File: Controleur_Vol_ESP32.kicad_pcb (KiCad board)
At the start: 2 copper layers, 67 parts, among them J1 Conn_01x03, J10 Conn_01x03, J11 Conn_01x08, J12 Conn_01x03, J13 Conn_01x03, J14 Conn_01x04, J15 Screw_Terminal_01x02, J2 Conn_01x03, J3 Conn_01x03, J4 Conn_01x03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

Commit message: Correction erreurs liens
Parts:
- moved J13 77.0 mm to (243.8, 238.8)
- moved J11 63.0 mm to (116.8, 275.6)
- moved J15 56.9 mm to (215.9, 236.2)
- moved J12 53.6 mm to (233.7, 248.9)
- moved U4 52.4 mm to (139.5, 272.2)
- moved R15 44.1 mm to (218.4, 264.2)
- moved R12 40.8 mm to (127.0, 233.7)
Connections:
- U4 pad 10: ESC3_5V -> ESC4_5V
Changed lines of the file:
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@@
   )
   (setup
+    (stackup
+      (layer "F.SilkS" (type "Top Silk Screen"))
+      (layer "F.Paste" (type "Top Solder Paste"))
+      (layer "F.Mask" (type "Top Solder Mask") (thickness 0.01))
+      (layer "F.Cu" (type "copper") (thickness 0.035))
+      (layer "dielectric 1" (type "core") (thickness 1.51) (material "FR4") (epsilon_r 4.5) (loss_tangent 0.02))
+      (layer "B.Cu" (type "copper") (thickness 0.035))
+      (layer "B.Mask" (type "Bottom Solder Mask") (thickness 0.01))
+      (layer "B.Paste" (type "Bottom Solder Paste"))
+      (layer "B.SilkS" (type "Bottom Silk Screen"))
+      (copper_finish "Immersion gold")
+      (dielectric_constraints no)
+    )
     (pad_to_mask_clearance 0)
     (pcbplotparams
@@
   )
   (footprint "Library_JBO:LM298_CI" (layer "F.Cu")
-    (at 127.25 221.23)
+    (at 139.455 272.225)
     (property "Sheetfile" "Controleur_Vol_ESP32.kicad_sch")
     (property "Sheetname" "")
@@
       (net 39 "ESC3_5V") (pinfunction "OUT3") (pintype "output"))
     (pad "10" thru_hole oval (at 2 19.5) (size 2 3.2) (drill 0.8) (layers *.Cu *.Mask)
-      (net 39 "ESC3_5V") (pinfunction "OUT4") (pintype "output"))
+      (net 41 "ESC4_5V") (pinfunction "OUT4") (pintype "output"))
   )
   (footprint "Resistor_SMD:R_1206_3216Metric_Pad1.30x1.75mm_HandSolder" (layer "F.Cu")
@@
   )
   (footprint "Resistor_SMD:R_1206_3216Metric_Pad1.30x1.75mm_HandSolder" (layer "F.Cu")
-    (at 164.385 249.975)
+    (at 127 233.68)
     (descr "Resistor SMD 1206 (3216 Metric), square (rectangular) end terminal, IPC_7351 nominal with elongated pad for handsoldering. (Body size source: IPC-SM-782 page 72, https://www.pcb-3d.com/wordpress/wp-content/uploads/ipc-sm-782a_amendment_1_and_2.pdf), generated with kicad-footprint-generator")
     (tags "resistor handsolder")
@@
   )
   (footprint "Resistor_SMD:R_1206_3216Metric_Pad1.30x1.75mm_HandSolder" (layer "F.Cu")
-    (at 192.285 228.705)
+    (at 218.44 264.16)
     (descr "Resistor SMD 1206 (3216 Metric), square (rectangular) end terminal, IPC_7351 nominal with elongated pad for handsoldering. (Body size source: IPC-SM-782 page 72, https://www.pcb-3d.com/wordpress/wp-content/uploads/ipc-sm-782a_amendment_1_and_2.pdf), generated with kicad-footprint-generator")
     (tags "resistor handsolder")
@@
   )
   (footprint "Connector_PinHeader_2.54mm:PinHeader_1x03_P2.54mm_Vertical" (layer "F.Cu")
-    (at 180.155 245.665)
+    (at 233.68 248.92)
     (descr "Through hole straight pin header, 1x03, 2.54mm pitch, single row")
     (tags "Through hole pin header THT 1x03 2.54mm single row")
@@
   )
   (footprint "TerminalBlock:TerminalBlock_bornier-2_P5.08mm" (layer "F.Cu")
-    (at 160.215 247.865)
+    (at 215.9 236.22)
     (descr "simple 2-pin terminal block, pitch 5.08mm, revamped version of bornier2")
     (tags "terminal block bornier2")
@@
   )
   (footprint "Connector_PinHeader_2.54mm:PinHeader_1x08_P2.54mm_Vertical" (layer "F.Cu")
-    (at 151.135 222.805)
+    (at 116.84 275.605)
     (descr "Through hole straight pin header, 1x08, 2.54mm pitch, single row")
     (tags "Through hole pin header THT 1x08 2.54mm single row")
@@
   )
   (footprint "Connector_PinHeader_2.54mm:PinHeader_1x03_P2.54mm_Vertical" (layer "F.Cu")
-    (at 168.605 255.365)
+    (at 243.84 238.76)
     (descr "Through hole straight pin header, 1x03, 2.54mm pitch, single row")
     (tags "Through hole pin header THT 1x03 2.54mm single row")

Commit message: 1er jet de routage
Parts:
- removed C1, C10, C11, C12, C14, C15, C21, C3, C4, C5, C6, C8, C9: 10nF, Capacitor_SMD:C_1206_3216Metric_Pad1.33x1.80mm_HandSolder
- removed J11: Conn_01x08, Connector_PinHeader_2.54mm:PinHeader_1x08_P2.54mm_Vertical
- removed R14, R15, R16, R17, R18, R9: 5k, Resistor_SMD:R_1206_3216Metric_Pad1.30x1.75mm_HandSolder
- added H1: MountingHole_Pad, MountingHole:MountingHole_4.3mm_M4, F.Cu at (97.8, 130.8)
- added H2: MountingHole_Pad, MountingHole:MountingHole_4.3mm_M4, F.Cu at (165.1, 130.8)
- added H3: MountingHole_Pad, MountingHole:MountingHole_4.3mm_M4, F.Cu at (97.8, 67.3)
- added H4: MountingHole_Pad, MountingHole:MountingHole_4.3mm_M4, F.Cu at (165.1, 67.3)
- added S1: 0, Resistor_SMD:R_1206_3216Metric_Pad1.30x1.75mm_HandSolder, B.Cu at (126.4, 92.7)
- added U2: MPU-6050_CI, Library_JBO:MPU-6050_CI, F.Cu at (110.4, 80.0)
- C13, C16, C17, C18, C19, C2, C20, C22, C23, C24, C7, R1, R19, R2, R20, R21, R22, R23, R3, R4, R6, R7, U3: moved to B.Cu
- R10, R11, R12, R13, R5, R8: value 5k -> 10k // 10nF; moved to B.Cu
- moved R19 187.4 mm to (132.7, 68.6)
- moved U1 182.8 mm to (124.5, 90.2)
- moved J15 181.9 mm to (145.4, 68.6)
- moved R20 179.8 mm to (125.7, 68.6)
- moved J14 179.3 mm to (85.1, 74.9), turned to -90 degrees
- moved R22 179.2 mm to (120.7, 75.6), turned to -90 degrees
- moved C17 178.9 mm to (116.8, 82.5)
- moved R1 173.3 mm to (108.0, 92.7)
- moved C2 168.8 mm to (100.3, 89.7)
- moved U4 167.2 mm to (142.1, 105.0), turned to 90 degrees
- moved C20 166.7 mm to (147.3, 87.6), turned to 90 degrees
- moved R8 164.0 mm to (115.6, 95.2)
- moved R21 162.4 mm to (123.2, 75.6), turned to -90 degrees
- moved U3 162.2 mm to (148.6, 76.2)
- moved R2 162.2 mm to (108.0, 95.2)
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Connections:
- J10 pad 3: Net-(J10-Pad3) -> GND
- J7 pad 3: Net-(J10-Pad3) -> GND
- J8 pad 3: Net-(J10-Pad3) -> GND
- J9 pad 3: Net-(J10-Pad3) -> GND
- R10 pad 2: Net-(R10-Pad2) -> GND
- R11 pad 2: Net-(R11-Pad2) -> GND
- R12 pad 2: Net-(R12-Pad2) -> GND
- R13 pad 2: Net-(R13-Pad2) -> GND
- R22 pad 2: SCL -> Net-(R22-Pad2)
- R5 pad 2: Net-(R5-Pad2) -> GND
- R8 pad 2: Net-(R14-Pad1) -> GND
- U1 pad 18: unconnected-(U1-Pad18) -> OUT6
- U1 pad 20: unconnected-(U1-Pad20) -> OUT5
- U1 pad 23: unconnected-(U1-Pad23) -> ESC4
- U1 pad 24: unconnected-(U1-Pad24) -> ESC3
- U1 pad 25: unconnected-(U1-Pad25) -> ESC2
- U1 pad 30: unconnected-(U1-Pad30) -> ESC1
- U4 pad 2: ESC1 -> GND
- U4 pad 3: (no net) -> ESC1
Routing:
- net +5V: track 0.00 -> 188.3 mm
- net +3.3V: track 0.00 -> 83.0 mm
- net VBATT: track 0.00 -> 69.9 mm
- net +VIN: track 0.00 -> 39.7 mm
- net ESC1_5V: track 0.00 -> 35.7 mm
- net SDA: track 0.00 -> 34.7 mm
- net ESC2_5V: track 0.00 -> 26.9 mm
- net OUT5: track 0.00 -> 19.7 mm
- net OUT6: track 0.00 -> 18.9 mm
- net Net-(R22-Pad2): track 0.00 -> 17.4 mm
- net ESC3_5V: track 0.00 -> 17.0 mm
- net ESC2: track 0.00 -> 14.3 mm
- net ESC3: track 0.00 -> 13.5 mm
- net ESC1: track 0.00 -> 12.9 mm
- net ESC4: track 0.00 -> 12.0 mm
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- added copper zone on B.Cu, net GND

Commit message: Ajout tearsdrop
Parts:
- turned C19 to 90 degrees

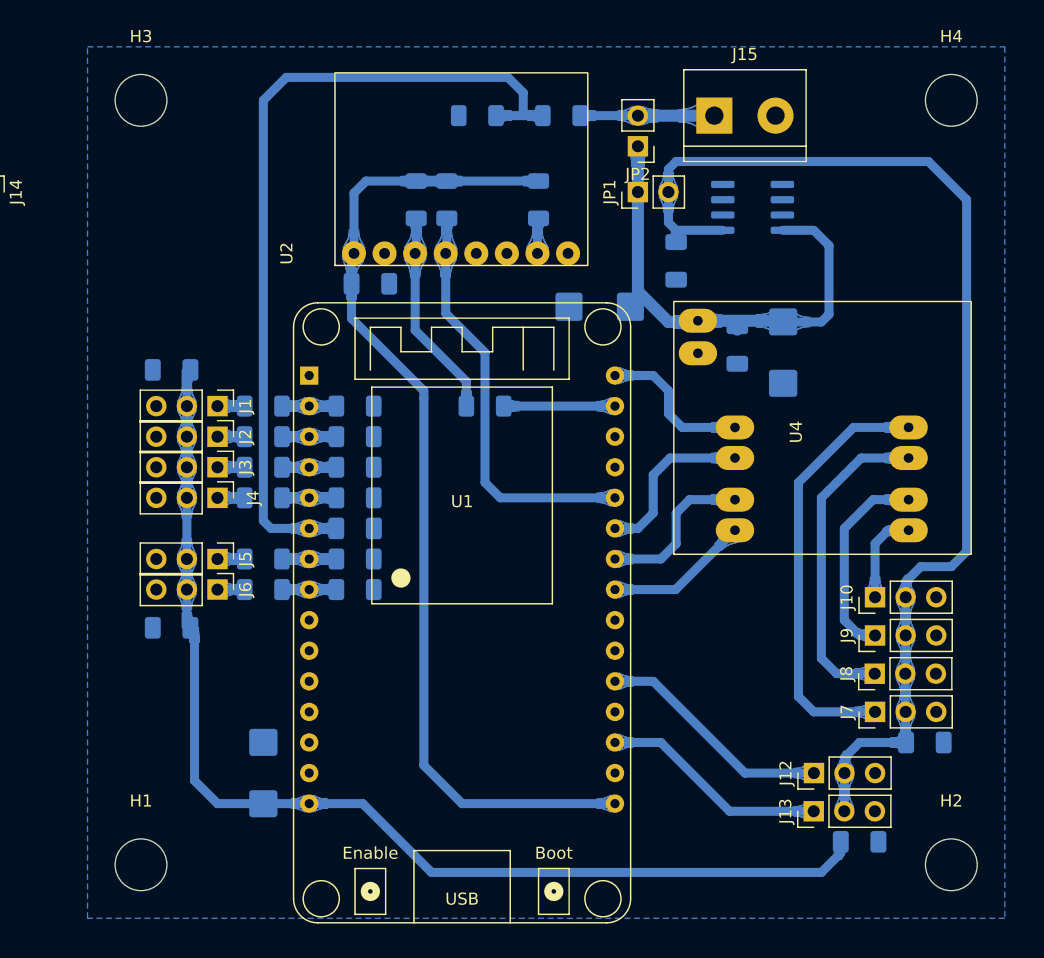
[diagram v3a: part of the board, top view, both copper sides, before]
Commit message: Straps maillage massage + contour PCB
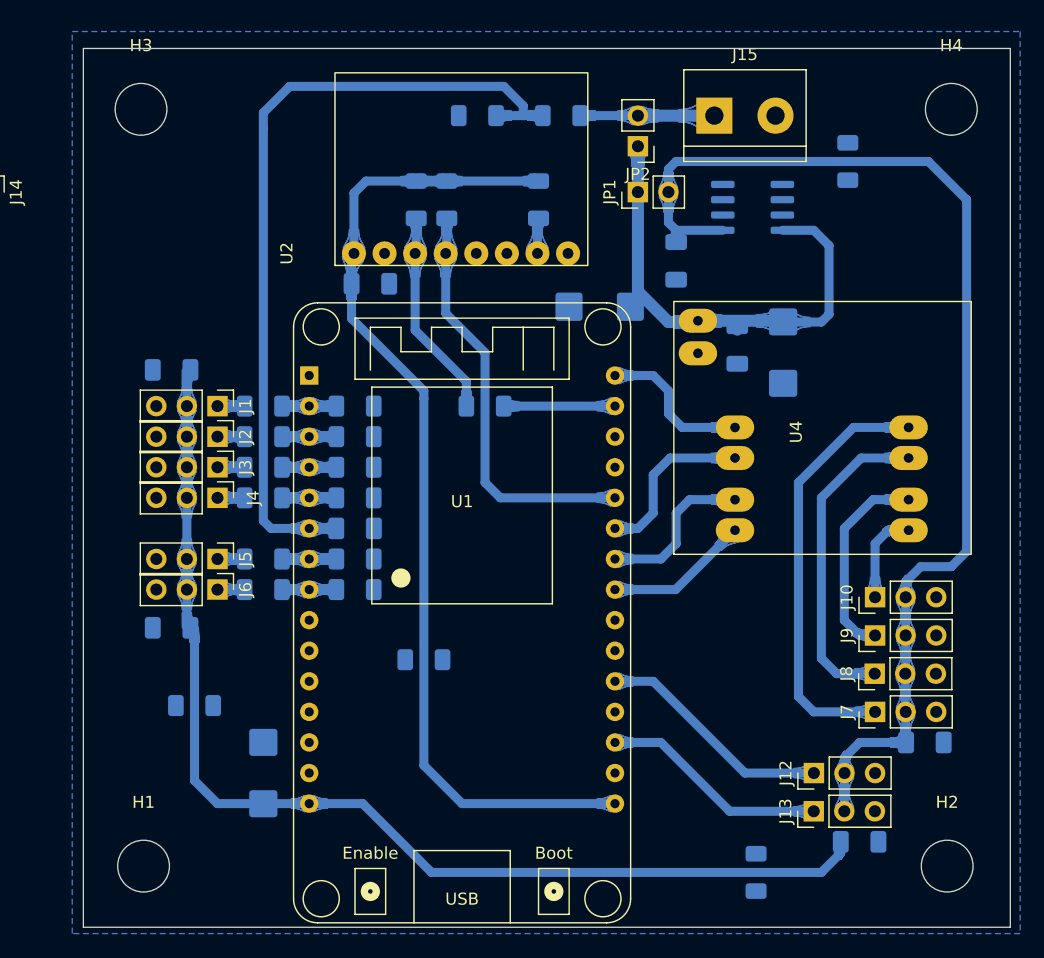
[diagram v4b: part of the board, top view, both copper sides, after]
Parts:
- added S2: 0, Resistor_SMD:R_1206_3216Metric_Pad1.30x1.75mm_HandSolder, B.Cu at (102.2, 117.6)
- added S3: 0, Resistor_SMD:R_1206_3216Metric_Pad1.30x1.75mm_HandSolder, B.Cu at (156.5, 72.4)
- added S4: 0, Resistor_SMD:R_1206_3216Metric_Pad1.30x1.75mm_HandSolder, B.Cu at (148.9, 131.4)
- added S5: 0, Resistor_SMD:R_1206_3216Metric_Pad1.30x1.75mm_HandSolder, B.Cu at (121.3, 113.8)
- moved H3 0.75 mm to (97.8, 68.1)
- moved H4 0.75 mm to (165.1, 68.1)
- moved H2 0.36 mm to (164.8, 130.9)
- moved H1 0.24 mm to (98.0, 130.9)
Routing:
- net VBATT: track 69.9 -> 68.1 mm
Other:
- board outline added: 77 x 73 mm

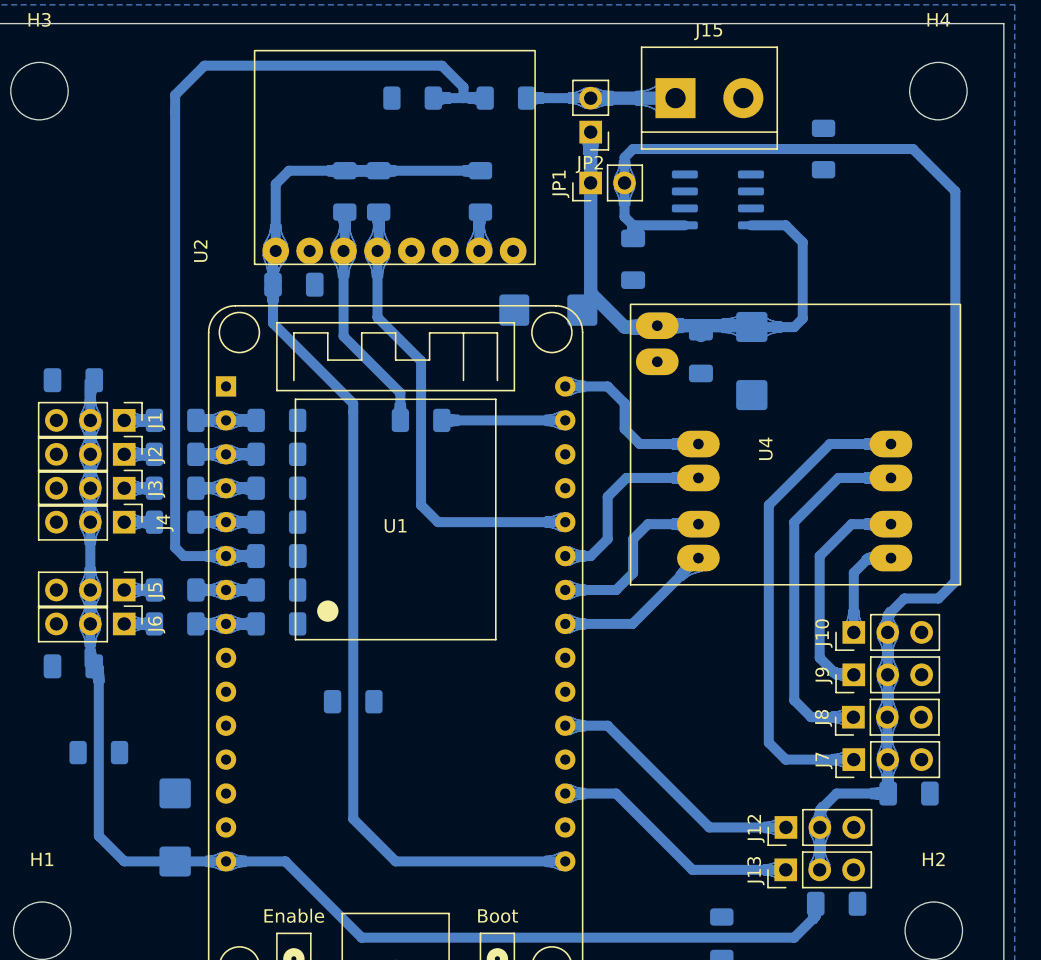
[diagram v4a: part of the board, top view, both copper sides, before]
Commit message: Ajout diodes "roue libre" sur sortie L293
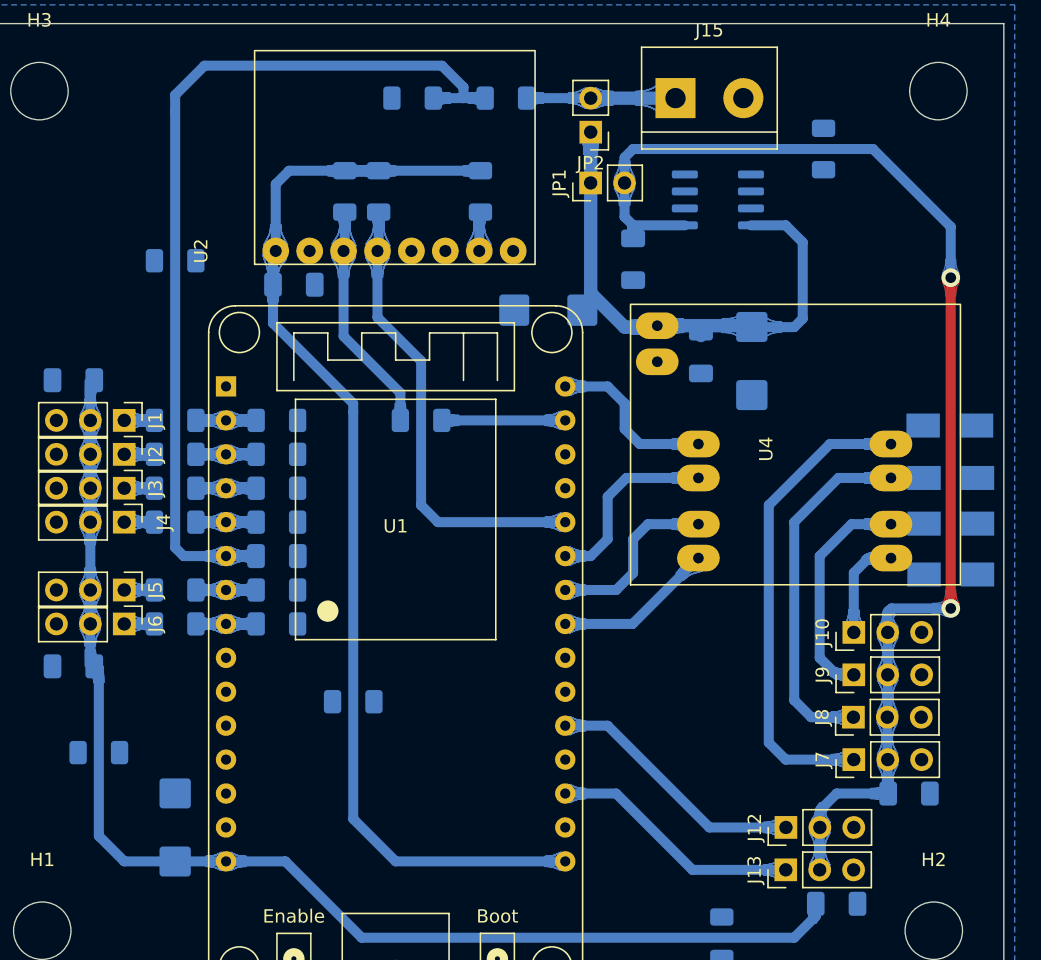
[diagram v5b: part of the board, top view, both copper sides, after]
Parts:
- added D1: US1M, Diode_SMD:D_SMA, B.Cu at (166.0, 93.1)
- added D2: US1M, Diode_SMD:D_SMA, B.Cu at (166.0, 97.0)
- added D3: US1M, Diode_SMD:D_SMA, B.Cu at (166.0, 100.4)
- added D4: US1M, Diode_SMD:D_SMA, B.Cu at (166.0, 104.2)
- added S6: 0, Resistor_SMD:R_1206_3216Metric_Pad1.30x1.75mm_HandSolder, B.Cu at (108.0, 80.8)
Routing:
- net +5V: track 188.3 -> 187.4 mm, vias 0 -> 2

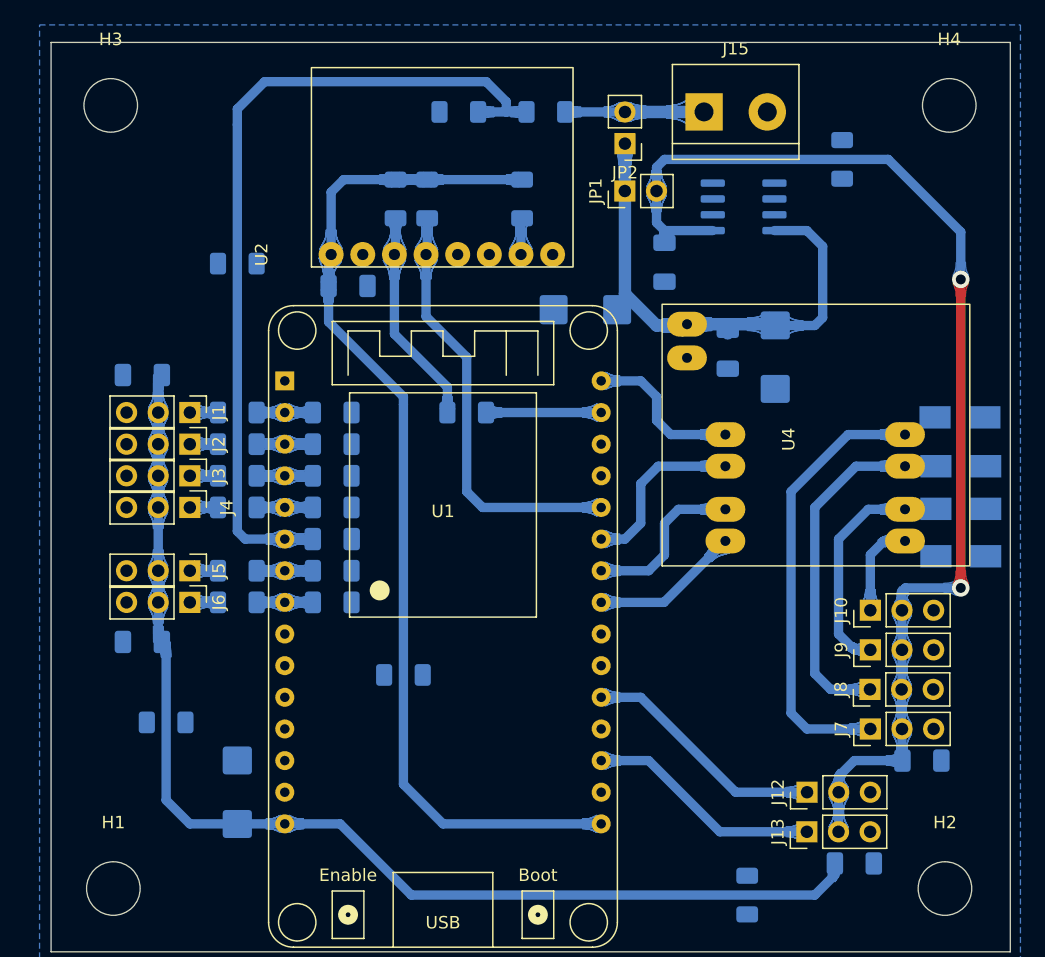
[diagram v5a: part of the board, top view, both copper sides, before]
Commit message: Ajout textes sur couche Top
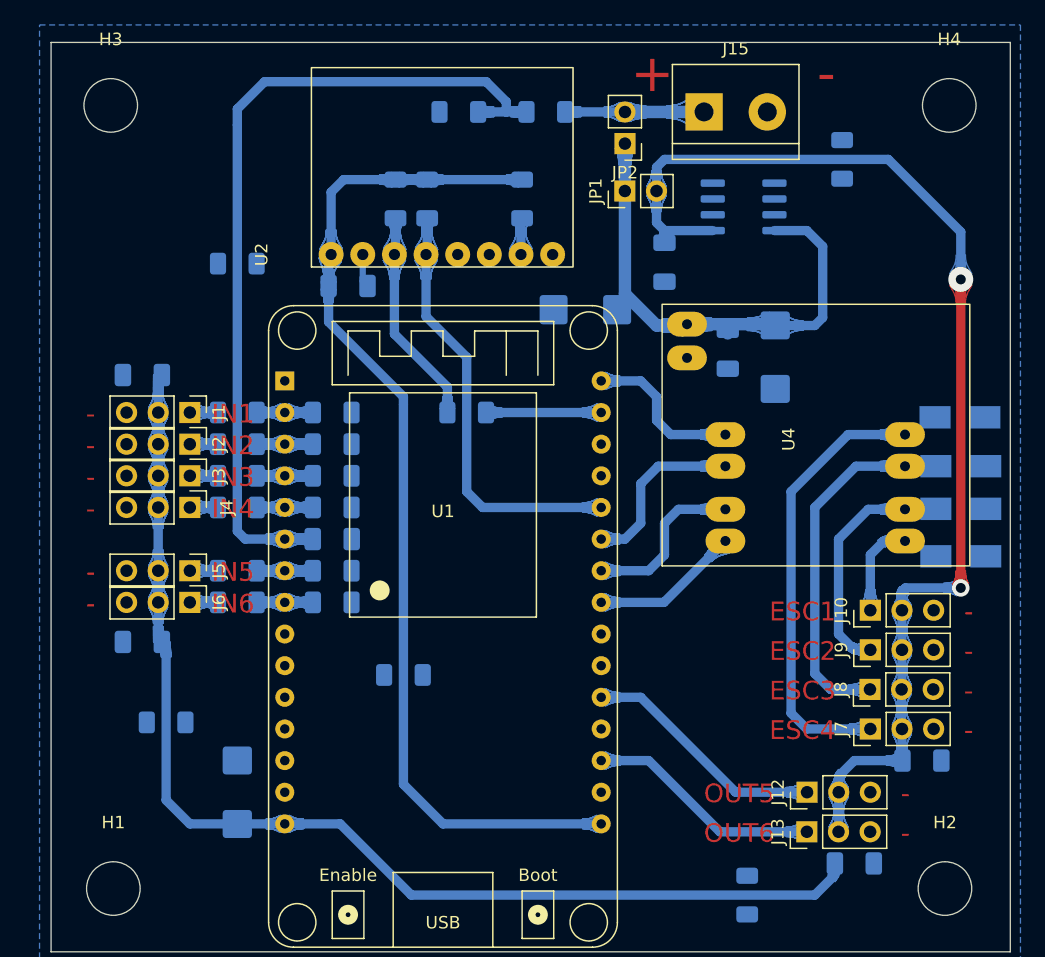
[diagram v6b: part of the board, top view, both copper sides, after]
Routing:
- net GND: track 0.00 -> 2.68 mm
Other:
- board text added: "+"
- board text added: "-"
- board text added: "ESC1"
- board text added: "ESC2"
- board text added: "ESC3"
- board text added: "ESC4"
- board text added: "IN1"
- board text added: "IN2"
- board text added: "IN3"
- board text added: "IN4"
- board text added: "IN5"
- board text added: "IN6"
- board text added: "OUT5"
- board text added: "OUT6"
